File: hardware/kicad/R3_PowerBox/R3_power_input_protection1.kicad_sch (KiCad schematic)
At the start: 13 parts, among them J1 SERVICE / BENCH INPUT 6-12V, Q1 DMP3007LSS-13

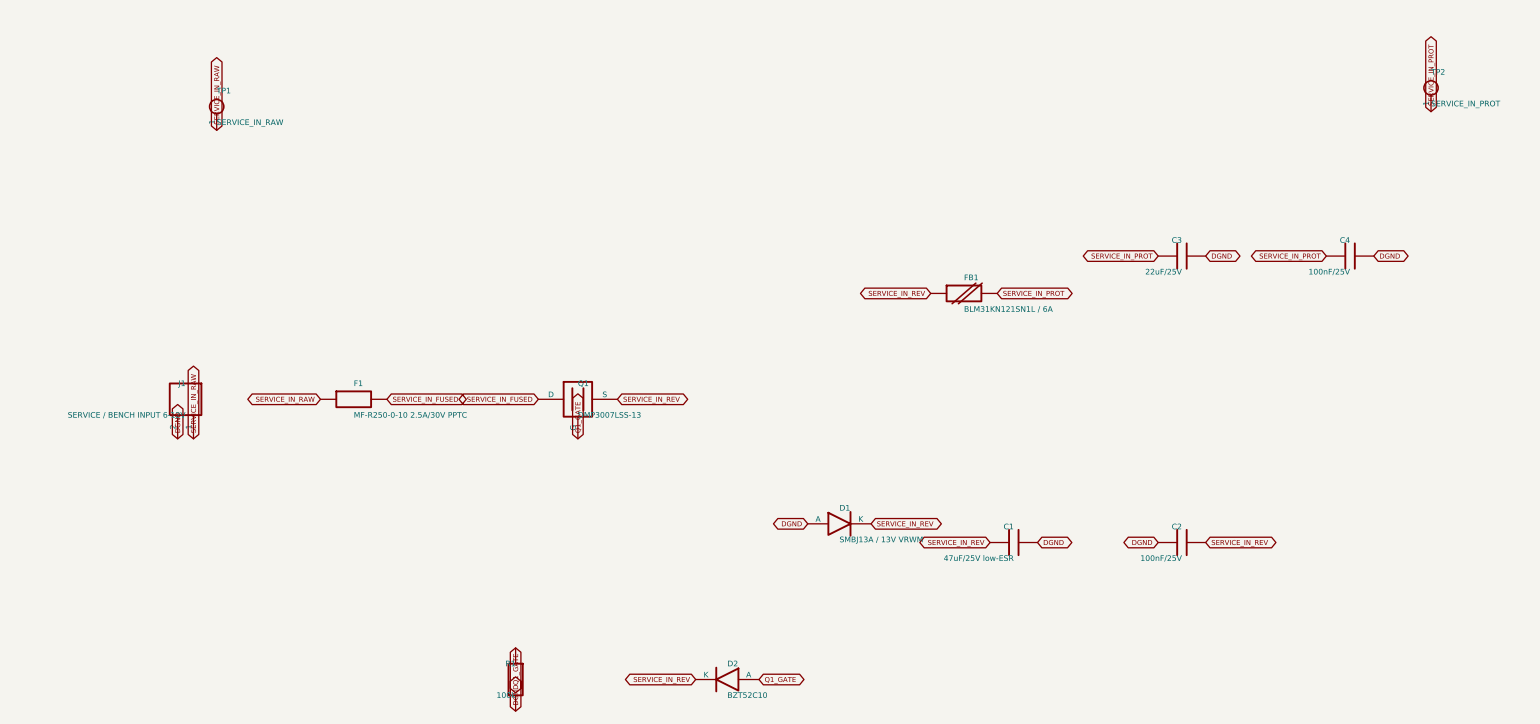
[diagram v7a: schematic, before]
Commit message: Rev.A review fixes: final CAD verification and documented hardware gates
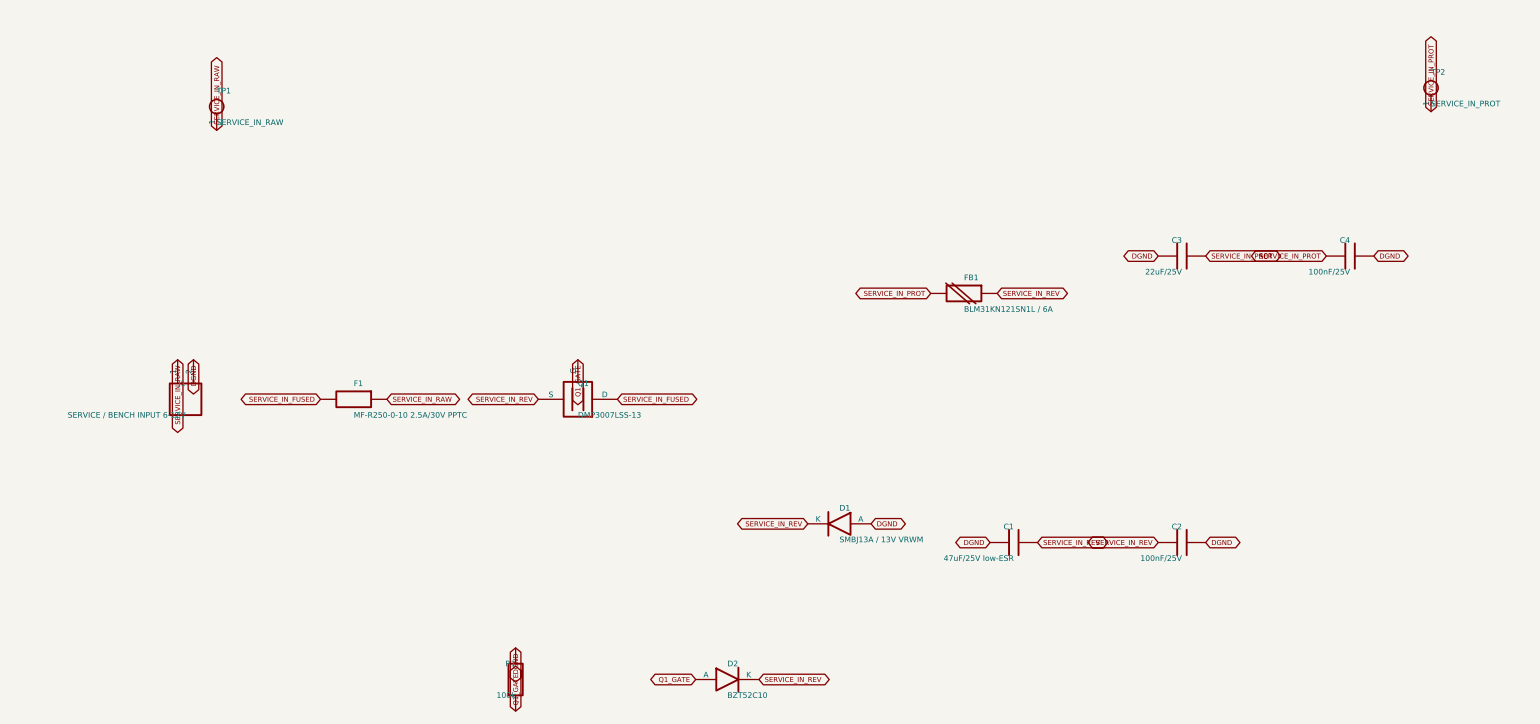
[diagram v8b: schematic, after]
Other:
- moved on the sheet: C1, C2, C3, D1, D2, F1, FB1, J1, Q1, R1
